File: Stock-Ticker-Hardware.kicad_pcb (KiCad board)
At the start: 2 copper layers, 0 parts

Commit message: Place on PCB
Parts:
- added A1: RaspberryPi_Pico_W, Module:RaspberryPi_Pico_W_SMD_HandSolder, F.Cu at (76.3, 80.0)
- added H1: MountingHole, MountingHole:MountingHole_2.7mm_M2.5, F.Cu at (54.0, 54.0)
- added H2: MountingHole, MountingHole:MountingHole_2.7mm_M2.5, F.Cu at (106.0, 54.0)
- added H3: MountingHole, MountingHole:MountingHole_2.7mm_M2.5, F.Cu at (54.0, 96.0)
- added H4: MountingHole, MountingHole:MountingHole_2.7mm_M2.5, F.Cu at (97.0, 96.0)
- added J1: Conn_01x05_Socket, Connector_JST:JST_XH_B5B-XH-A_1x05_P2.50mm_Vertical, F.Cu at (97.5, 56.0)
- added SW1: SW_Push, Button_Switch_THT:SW_PUSH-12mm, F.Cu at (59.8, 57.5)
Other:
- board outline added: 60 x 50 mm

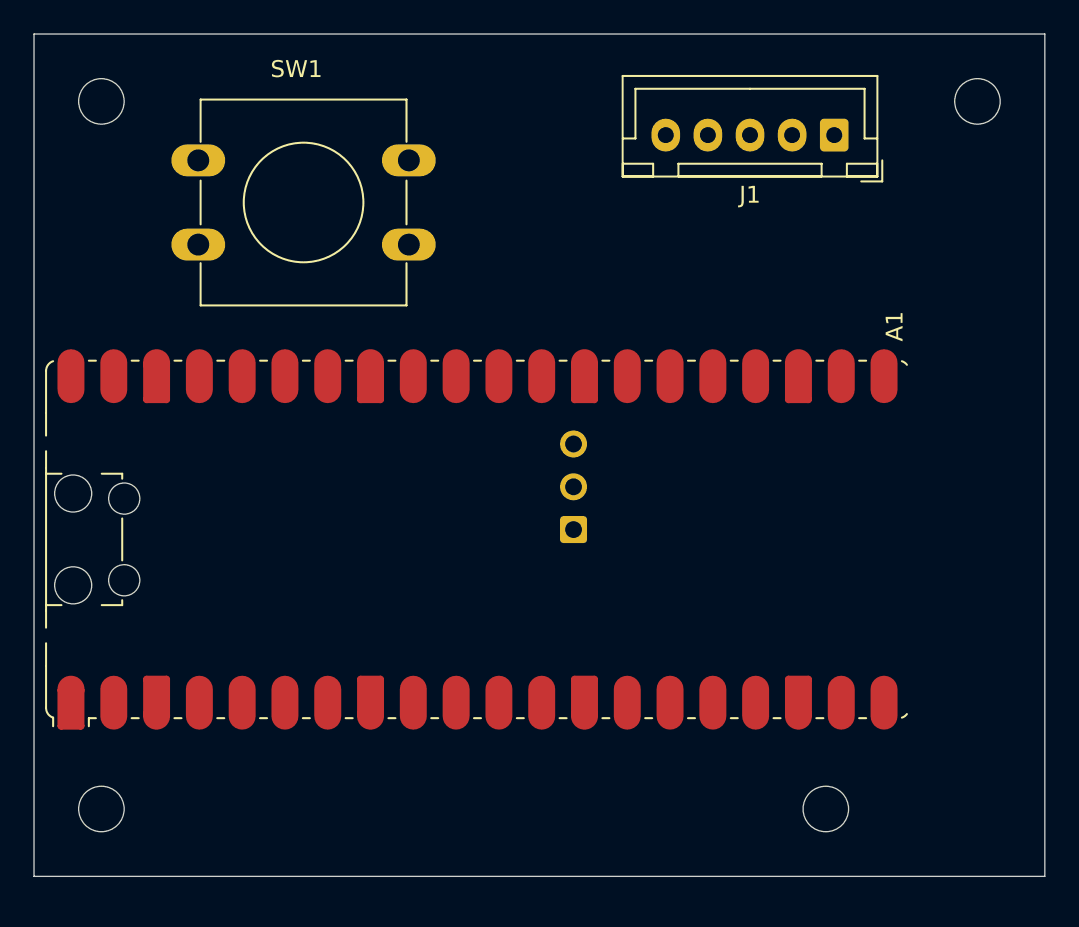
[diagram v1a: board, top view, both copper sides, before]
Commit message: Add connectors for SWD and UART for easy debugging
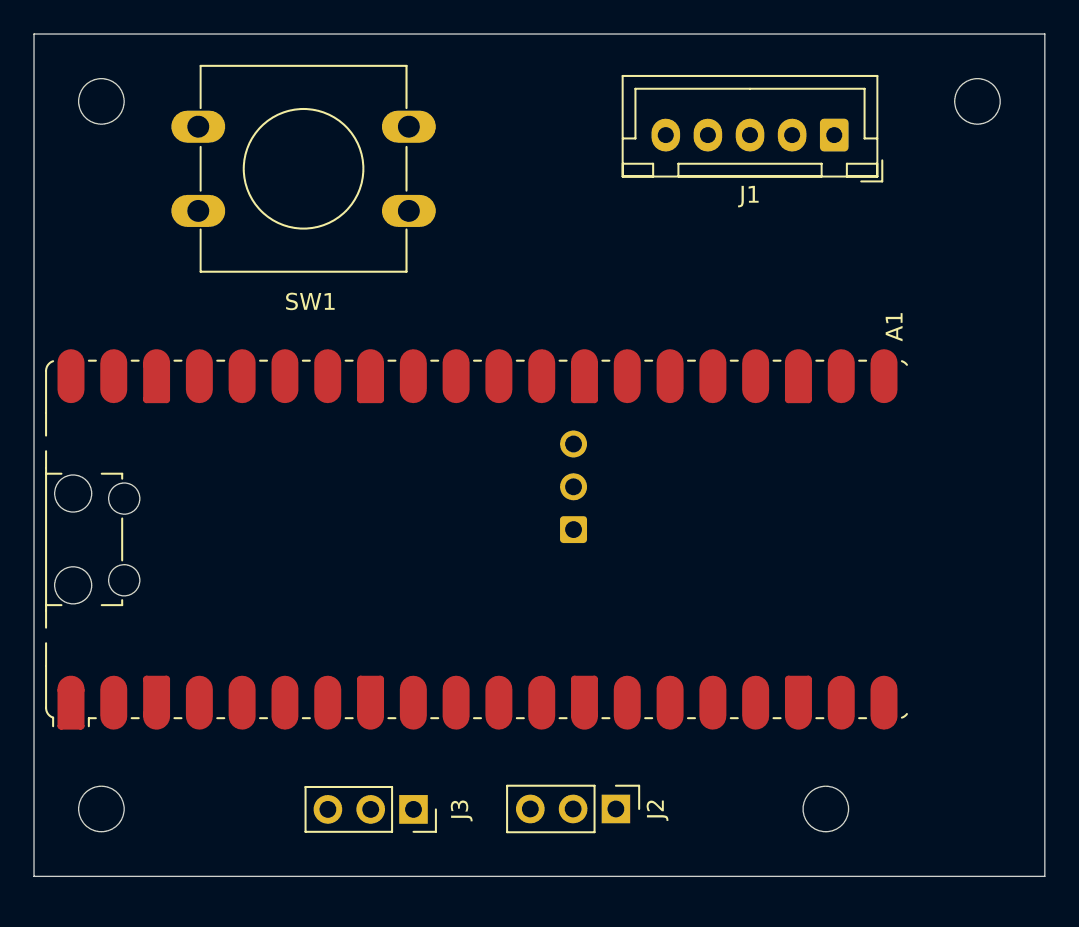
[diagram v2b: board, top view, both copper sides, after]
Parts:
- added J2: Conn_01x03_Pin, Connector_PinHeader_2.54mm:PinHeader_1x03_P2.54mm_Vertical, F.Cu at (84.5, 96.0)
- added J3: Conn_01x03_Socket, Connector_PinSocket_2.54mm:PinSocket_1x03_P2.54mm_Vertical, F.Cu at (72.5, 96.0)
- moved SW1 12.9 mm to (72.2, 60.5), turned to 180 degrees
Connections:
- A1 pad 1: unconnected-(A1-GPIO0-Pad1) -> /UART0_TX
- A1 pad 2: unconnected-(A1-GPIO1-Pad2) -> /UART0_RX
- A1 pad D1: unconnected-(A1-SWCLK-PadD1) -> /SWCLK
- A1 pad D3: unconnected-(A1-SWDIO-PadD3) -> /SWDIO

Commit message: Finish simple PCB
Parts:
- moved J3 8.23 mm to (64.5, 94.0)
- moved J2 6.32 mm to (78.5, 94.0)
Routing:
- net GND: track 0.00 -> 153.9 mm
- net Net-(A1-GPIO17): track 0.00 -> 62.2 mm, vias 0 -> 1
- net /CLK: track 0.00 -> 53.0 mm, vias 0 -> 1
- net /DOUT: track 0.00 -> 46.2 mm, vias 0 -> 1
- net /CS: track 0.00 -> 45.1 mm, vias 0 -> 1
- net +5V: track 0.00 -> 41.7 mm
- net /SWDIO: track 0.00 -> 23.2 mm
- net /SWCLK: track 0.00 -> 16.0 mm
- net /UART0_RX: track 0.00 -> 12.5 mm
- net /UART0_TX: track 0.00 -> 10.0 mm
- added copper zone on B.Cu, net GND
- added copper zone on F.Cu, net GND
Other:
- board text added: "5V"
- board text added: "CLK"
- board text added: "CS"
- board text added: "DIO"
- board text added: "DOUT"
- board text added: "GND"
- board text added: "MAX7219 line"
- board text added: "RX"
- board text added: "SWD"
- board text added: "TX"
- board text added: "UART"

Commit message: Better schematic with level shifter, decoup caps, delete PCB
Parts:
- removed A1: RaspberryPi_Pico_W, Module:RaspberryPi_Pico_W_SMD_HandSolder
- removed H1, H2, H3, H4: MountingHole, MountingHole:MountingHole_2.7mm_M2.5
- removed J1: Conn_01x05_Socket, Connector_JST:JST_XH_B5B-XH-A_1x05_P2.50mm_Vertical
- removed J2: Conn_01x03_Pin, Connector_PinHeader_2.54mm:PinHeader_1x03_P2.54mm_Vertical
- removed J3: Conn_01x03_Socket, Connector_PinSocket_2.54mm:PinSocket_1x03_P2.54mm_Vertical
- removed SW1: SW_Push, Button_Switch_THT:SW_PUSH-12mm
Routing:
- net GND: track 153.9 -> 0.00 mm
- net Net-(A1-GPIO17): track 62.2 -> 0.00 mm, vias 1 -> 0
- net /CLK: track 53.0 -> 0.00 mm, vias 1 -> 0
- net /DOUT: track 46.2 -> 0.00 mm, vias 1 -> 0
- net /CS: track 45.1 -> 0.00 mm, vias 1 -> 0
- net +5V: track 41.7 -> 0.00 mm
- net /SWDIO: track 23.2 -> 0.00 mm
- net /SWCLK: track 16.0 -> 0.00 mm
- net /UART0_RX: track 12.5 -> 0.00 mm
- net /UART0_TX: track 10.0 -> 0.00 mm
- removed copper zone on B.Cu, net GND
- removed copper zone on F.Cu, net GND
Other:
- board outline removed
- board text removed: "5V"
- board text removed: "CLK"
- board text removed: "CS"
- board text removed: "DIO"
- board text removed: "DOUT"
- board text removed: "GND"
- board text removed: "MAX7219 line"
- board text removed: "RX"
- board text removed: "SWD"
- board text removed: "TX"
- board text removed: "UART"

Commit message: Component layout once again
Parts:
- added A1: RaspberryPi_Pico_W, Module:RaspberryPi_Pico_W_SMD_HandSolder, F.Cu at (76.1, 80.7)
- added C1: 0.1 uF, Capacitor_THT:C_Disc_D5.0mm_W2.5mm_P2.50mm, F.Cu at (78.5, 63.8)
- added C2: 0.1 uF, Capacitor_THT:C_Disc_D5.0mm_W2.5mm_P2.50mm, F.Cu at (78.5, 54.0)
- added C3: C_Polarized, Capacitor_THT:CP_Radial_D4.0mm_P2.00mm, F.Cu at (78.0, 57.2)
- added H1: MountingHole, MountingHole:MountingHole_2.7mm_M2.5, F.Cu at (54.0, 54.0)
- added H2: MountingHole, MountingHole:MountingHole_2.7mm_M2.5, F.Cu at (99.0, 54.0)
- added H3: MountingHole, MountingHole:MountingHole_2.7mm_M2.5, F.Cu at (54.0, 96.0)
- added H4: MountingHole, MountingHole:MountingHole_2.7mm_M2.5, F.Cu at (99.0, 96.0)
- added J1: Conn_01x05_Socket, Connector_JST:JST_XH_B5B-XH-A_1x05_P2.50mm_Vertical, F.Cu at (93.0, 54.0)
- added J2: Conn_01x03_Pin, Connector_PinHeader_2.54mm:PinHeader_1x03_P2.54mm_Vertical, F.Cu at (77.6, 94.5)
- added J3: Conn_01x03_Socket, Connector_PinSocket_2.54mm:PinSocket_1x03_P2.54mm_Vertical, F.Cu at (65.6, 94.5)
- added SW1: SW_Push, Button_Switch_THT:SW_PUSH-12mm, F.Cu at (71.2, 60.0)
- added U1: 74AHCT125, Package_DIP:DIP-14_W7.62mm, F.Cu at (83.4, 66.8)
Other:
- board outline added: 53 x 50 mm

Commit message: Finish routing
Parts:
- moved C3 2.74 mm to (75.4, 56.4)
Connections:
- A1 pad 22: Net-(A1-GPIO17) -> unconnected-(A1-GPIO17-Pad22)
- A1 pad 29: unconnected-(A1-GPIO22-Pad29) -> Net-(A1-GPIO22)
- SW1 pad 1: Net-(A1-GPIO17) -> Net-(A1-GPIO22)
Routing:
- net GND: track 0.00 -> 230.8 mm
- net +5V: track 0.00 -> 59.4 mm
- net /DOUT: track 0.00 -> 48.7 mm, vias 0 -> 1
- net /CS: track 0.00 -> 37.6 mm, vias 0 -> 1
- net /CLK: track 0.00 -> 37.0 mm, vias 0 -> 1
- net Net-(A1-GPIO22): track 0.00 -> 34.6 mm, vias 0 -> 1
- net /SWDIO: track 0.00 -> 23.3 mm
- net Net-(J1-Pin_1): track 0.00 -> 19.5 mm
- net /SWCLK: track 0.00 -> 16.2 mm
- net Net-(J1-Pin_2): track 0.00 -> 15.1 mm
- net /UART0_RX: track 0.00 -> 13.0 mm
- net Net-(J1-Pin_3): track 0.00 -> 12.8 mm
- net /UART0_TX: track 0.00 -> 10.4 mm
- added copper zone on B.Cu, net GND
- added copper zone on F.Cu, net GND

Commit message: Finish actual routing this time
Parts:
- added C4: 0.1 μF, Capacitor_THT:C_Disc_D5.0mm_W2.5mm_P2.50mm, F.Cu at (76.2, 54.8)
- added R1: 10 kΩ, Resistor_THT:R_Axial_DIN0207_L6.3mm_D2.5mm_P10.16mm_Horizontal, F.Cu at (61.0, 67.0)
- added R2: 1 kΩ, Resistor_THT:R_Axial_DIN0207_L6.3mm_D2.5mm_P10.16mm_Horizontal, F.Cu at (76.2, 67.7)
- C1, C2: value 0.1 uF -> 0.1 μF
- C3: value C_Polarized -> 10 μF
- moved C1 8.14 mm to (82.4, 56.6), turned to 180 degrees
- moved H4 8.00 mm to (107.0, 96.0)
- moved H2 7.00 mm to (106.0, 54.0)
- moved J1 7.00 mm to (100.0, 54.0)
- moved C2 6.91 mm to (85.4, 54.5)
- moved C3 6.54 mm to (81.4, 53.8), turned to 90 degrees
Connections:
- A1 pad 36: unconnected-(A1-3V3-Pad36) -> +3.3V
- SW1 pad 1: Net-(A1-GPIO22) -> Net-(C4-Pad1)
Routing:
- net GND: track 230.8 -> 192.5 mm
- net Net-(A1-GPIO22): track 34.6 -> 5.53 mm, vias 1 -> 0
- net Net-(C4-Pad1): track 0.00 -> 28.3 mm
- net Net-(J1-Pin_3): track 12.8 -> 6.66 mm
- net +3.3V: track 0.00 -> 4.46 mm
- net +5V: track 59.4 -> 58.3 mm
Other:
- board size 53 x 50 mm -> 60 x 50 mm

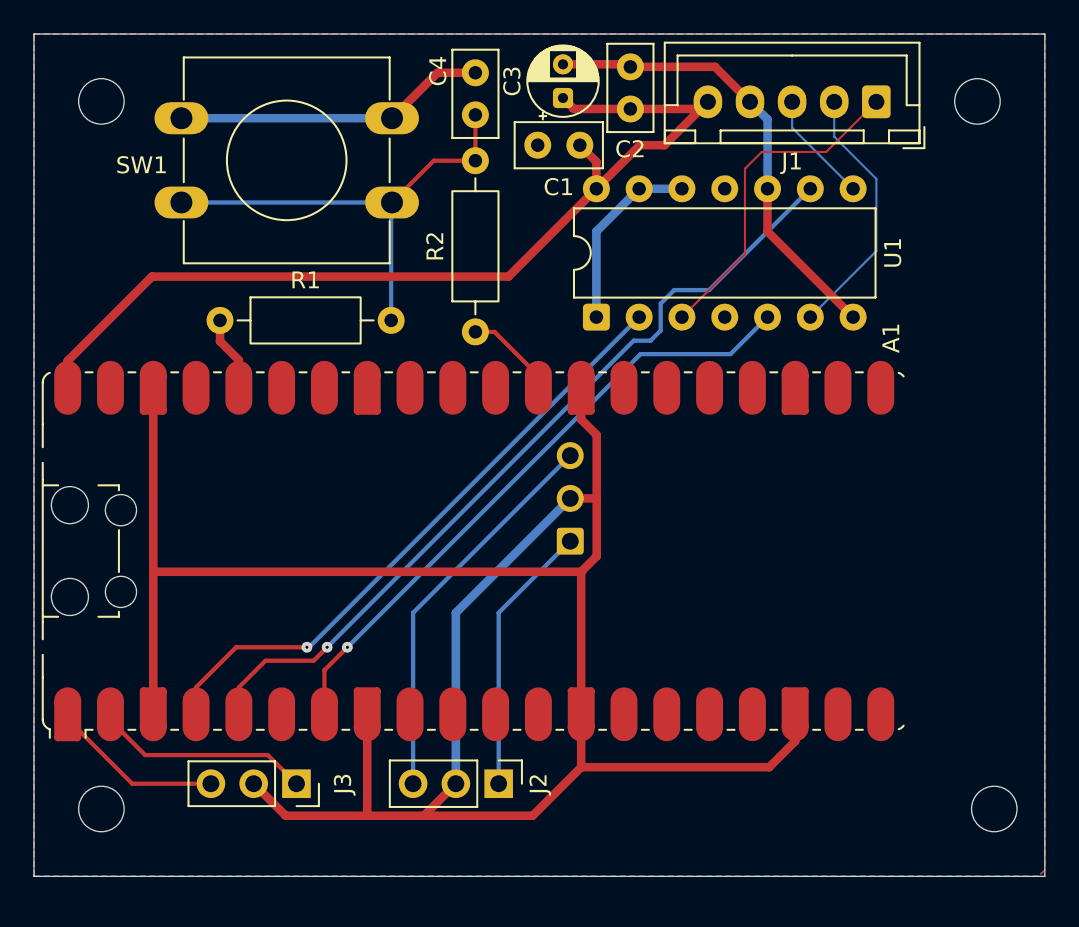
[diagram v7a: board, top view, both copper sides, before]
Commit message: Increase 5v trace width
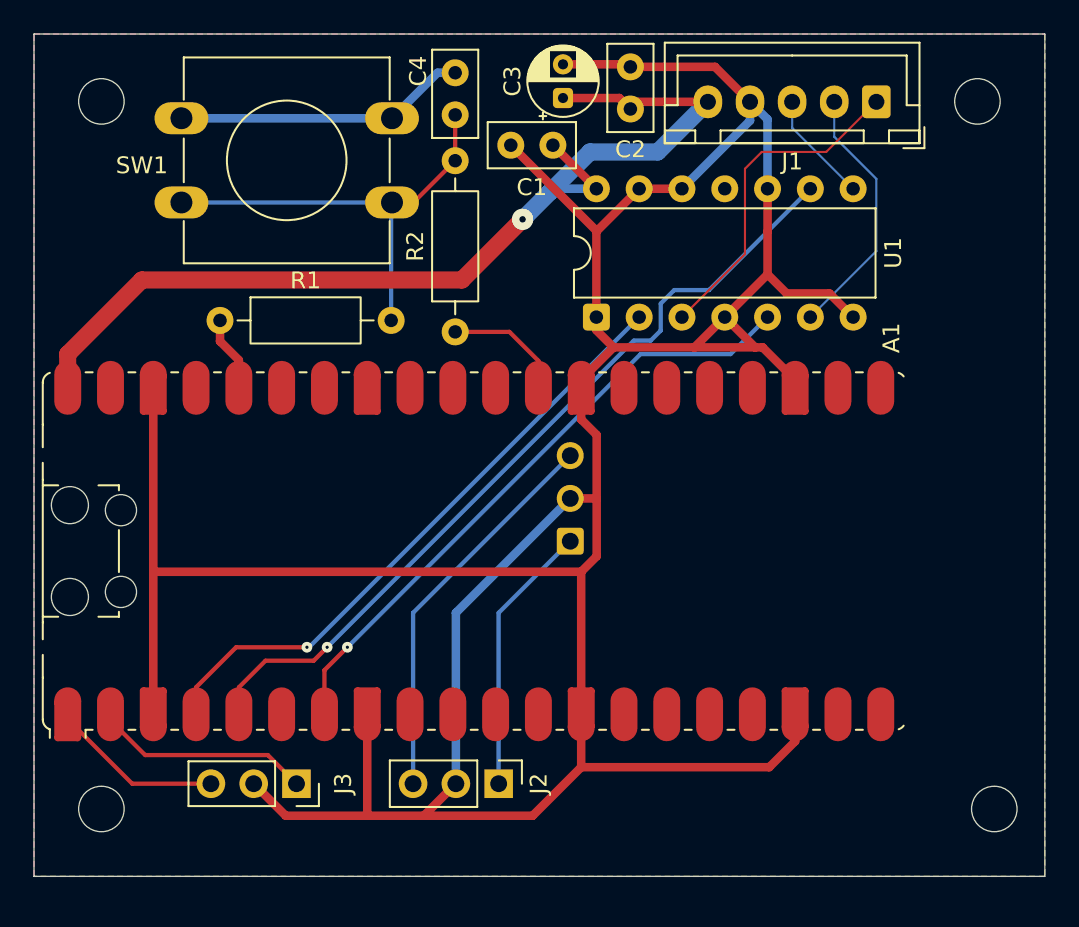
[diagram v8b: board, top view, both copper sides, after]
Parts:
- moved C1 1.60 mm to (80.8, 56.6)
- moved C4 1.20 mm to (75.0, 54.8)
- moved R2 1.20 mm to (75.0, 67.7)
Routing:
- net GND: track 192.5 -> 233.0 mm
- net +5V: track 58.3 -> 62.7 mm, vias 0 -> 1
- net Net-(A1-GPIO22): track 5.53 -> 7.25 mm
- net Net-(C4-Pad1): track 28.3 -> 27.1 mm
